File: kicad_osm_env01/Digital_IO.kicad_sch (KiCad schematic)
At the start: 22 parts, among them U18 MIC94073YC6, U20 MIC94073YC6

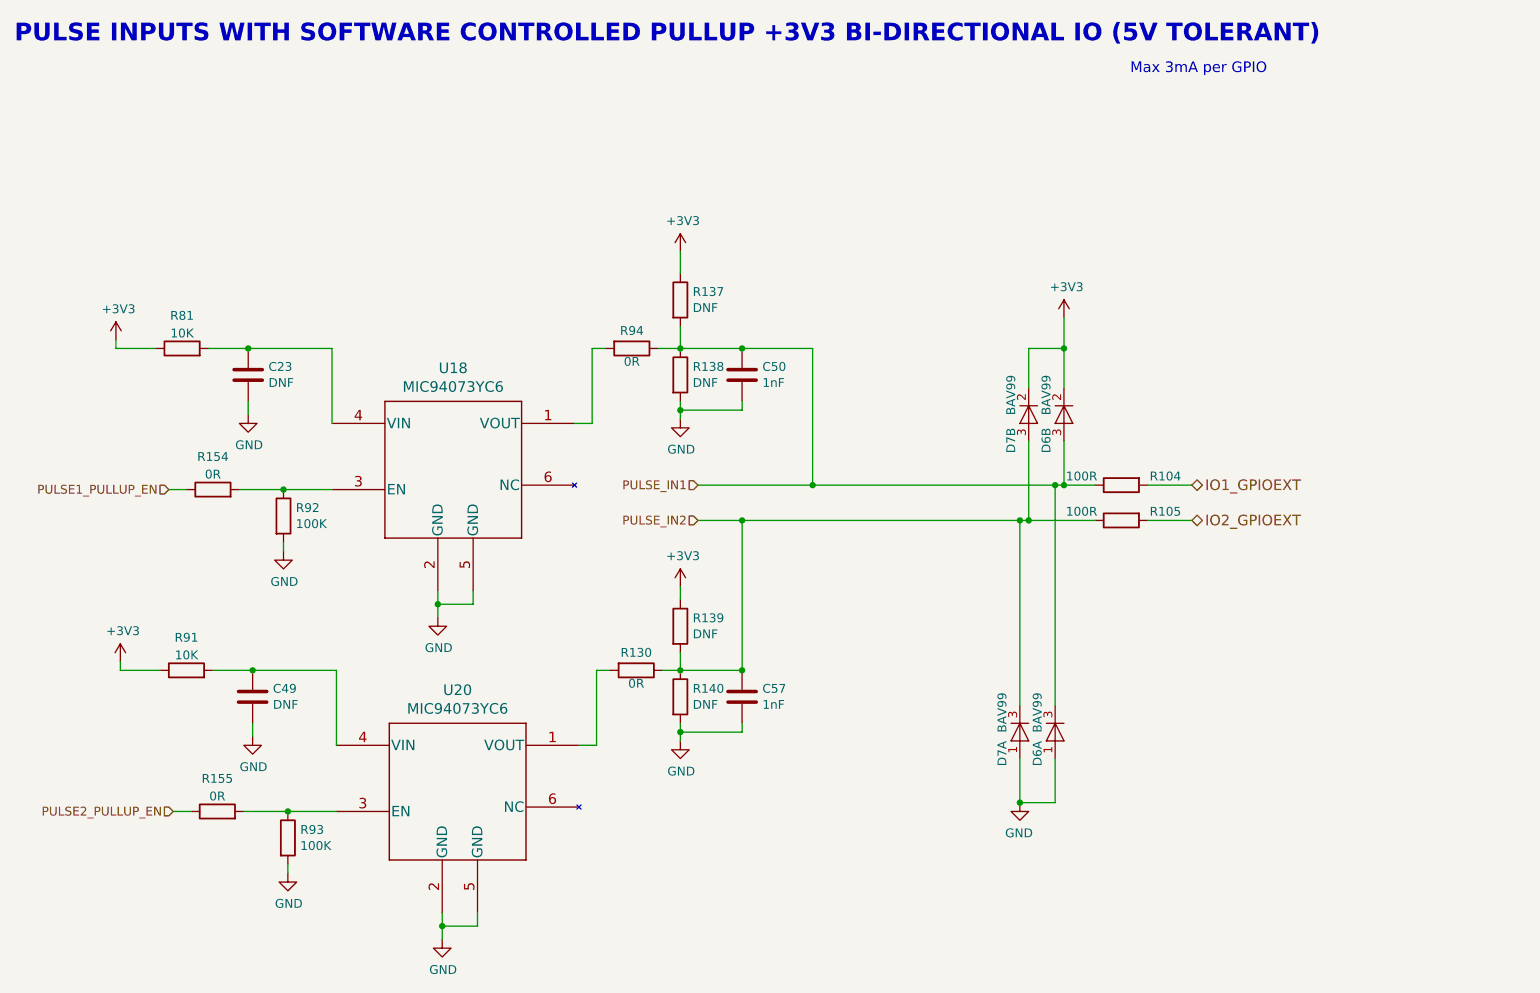
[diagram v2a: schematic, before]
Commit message: updated schematics
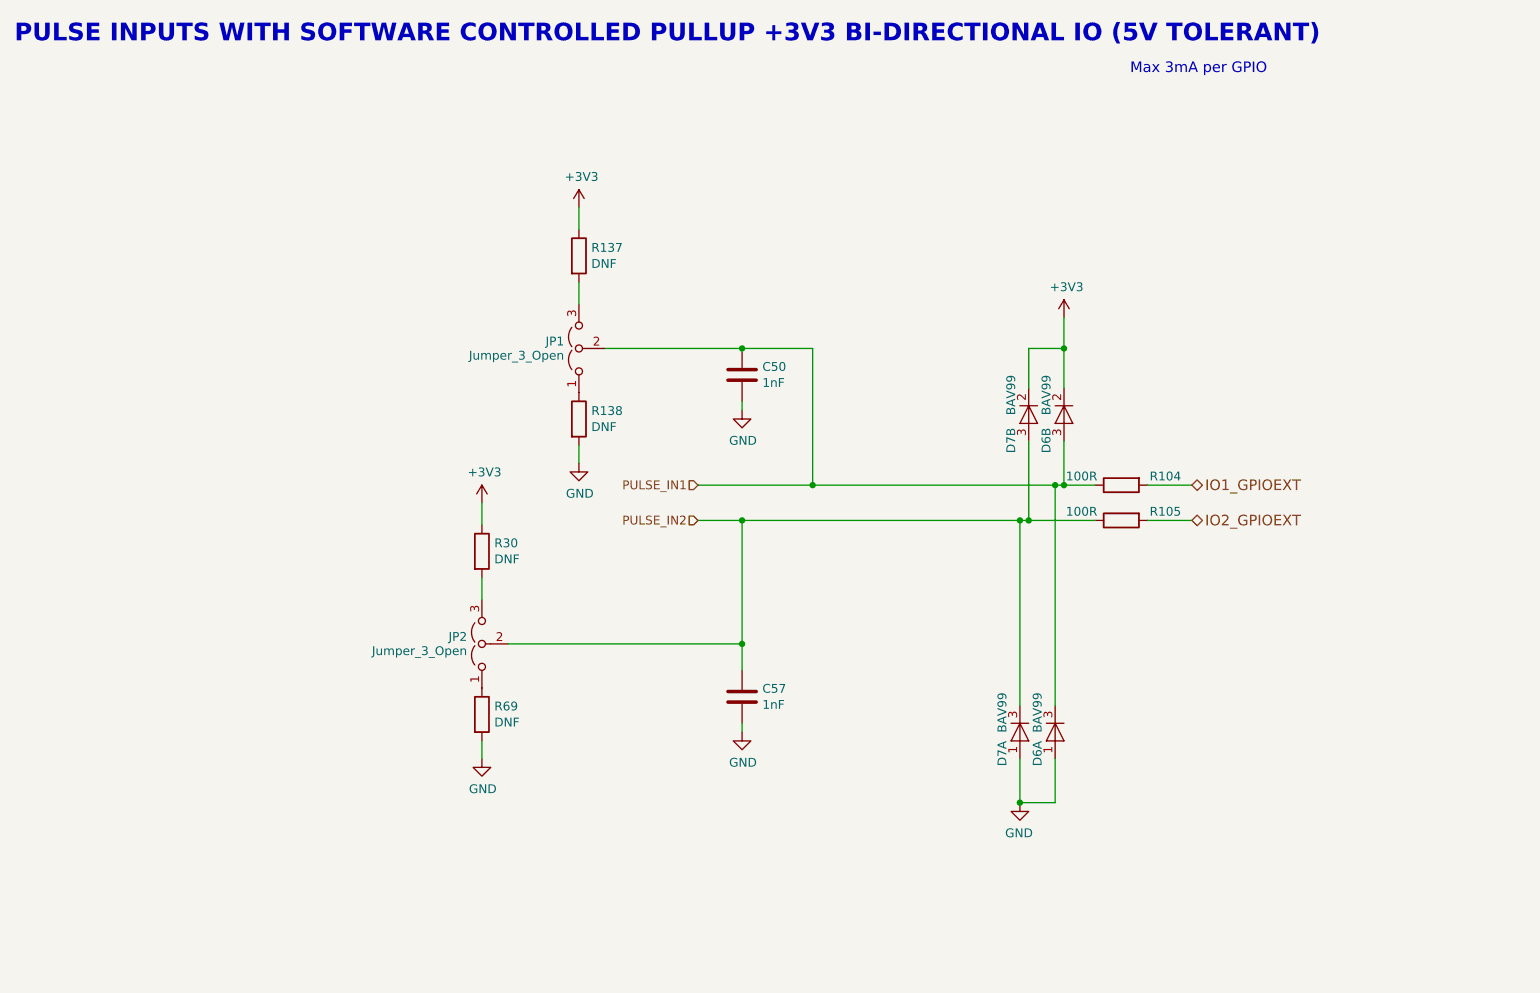
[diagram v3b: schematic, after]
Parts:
- removed C23, C49: DNF, Capacitor_SMD:C_0402_1005Metric, symbol Device:C
- removed R130, R154, R155, R94: 0R, Resistor_SMD:R_0402_1005Metric, symbol Device:R
- removed R139, R140: DNF, Resistor_SMD:R_0402_1005Metric, symbol Device:R
- removed R81, R91: 10K, Resistor_SMD:R_0402_1005Metric, symbol Device:R
- removed R92, R93: 100K, Resistor_SMD:R_0402_1005Metric, symbol Device:R
- removed U18, U20: MIC94073YC6, Package_TO_SOT_SMD:SOT-363_SC-70-6, symbol Devtank:MIC94073YC6
- added JP1, JP2: Jumper_3_Open, symbol Jumper:Jumper_3_Open
- added R30, R69: DNF, Resistor_SMD:R_0402_1005Metric, symbol Device:R
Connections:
- net +3V3: now also R30.1
- net GND: now also R69.2
- net PULSE_IN1: now also JP1.2 (C); no longer R137.2, R138.1
- net PULSE_IN2: now also JP2.2 (C)
- new net: JP2.1 (A), R69.1
- new net: JP2.3 (B), R30.2
- new net: JP1.1 (A), R138.1
- new net: JP1.3 (B), R137.2
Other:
- moved on the sheet: R137, R138

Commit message: added tracking to layout
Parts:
- removed JP1, JP2: Jumper_3_Open, symbol Jumper:Jumper_3_Open
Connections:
- net PULSE_IN1: now also R137.2, R138.1
- net PULSE_IN2: now also R30.2, R69.1
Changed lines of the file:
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@@
   (junction (at 203.835 130.81) (diameter 0) (color 0 0 0 0)
   )
+  (junction (at 140.335 65.405) (diameter 0) (color 0 0 0 0)
+  )
+  (junction (at 126.365 107.95) (diameter 0) (color 0 0 0 0)
+  )
   (junction (at 210.185 85.09) (diameter 0) (color 0 0 0 0)
   )
@@
     (stroke (width 0) (type default))
   )
-  (wire (pts (xy 126.365 98.425) (xy 126.365 101.6))
+  (wire (pts (xy 126.365 98.425) (xy 126.365 107.95))
     (stroke (width 0) (type default))
   )
@@
     (stroke (width 0) (type default))
   )
+  (wire (pts (xy 126.365 107.95) (xy 163.83 107.95))
+    (stroke (width 0) (type default))
+  )
   (wire (pts (xy 163.83 65.405) (xy 173.99 65.405))
     (stroke (width 0) (type default))
@@
     (stroke (width 0) (type default))
   )
-  (wire (pts (xy 144.145 65.405) (xy 163.83 65.405))
+  (wire (pts (xy 140.335 65.405) (xy 163.83 65.405))
     (stroke (width 0) (type default))
   )
@@
     (stroke (width 0) (type default))
   )
+  (wire (pts (xy 140.335 65.405) (xy 140.335 71.755))
+    (stroke (width 0) (type default))
+  )
+  (wire (pts (xy 126.365 107.95) (xy 126.365 114.3))
+    (stroke (width 0) (type default))
+  )
   (wire (pts (xy 210.185 71.12) (xy 210.185 65.405))
     (stroke (width 0) (type default))
@@
     (stroke (width 0) (type default))
   )
-  (wire (pts (xy 140.335 55.88) (xy 140.335 59.055))
+  (wire (pts (xy 140.335 55.88) (xy 140.335 65.405))
     (stroke (width 0) (type default))
   )
@@
   )
   (wire (pts (xy 210.185 65.405) (xy 205.105 65.405))
-    (stroke (width 0) (type default))
-  )
-  (wire (pts (xy 130.175 107.95) (xy 163.83 107.95))
     (stroke (width 0) (type default))
   )
@@
     )
   )
-  (symbol (lib_id "Jumper:Jumper_3_Open") (at 140.335 65.405 90) (unit 1)
-    (in_bom yes) (on_board yes) (dnp no) (fields_autoplaced)
-    (property "Reference" "JP1" (at 138.2009 64.381 90)
-      (effects (font (size 1.27 1.27)) (justify left))
-    )
-    (property "Value" "Jumper_3_Open" (at 138.2009 66.429 90)
-      (effects (font (size 1.27 1.27)) (justify left))
-    )
-    (property "Footprint" "" (at 140.335 65.405 0)
-      (effects (font (size 1.27 1.27)) hide)
-    )
-    (property "Datasheet" "~" (at 140.335 65.405 0)
-      (effects (font (size 1.27 1.27)) hide)
-    )
-    (pin "1")
-    (pin "2")
-    (pin "3")
-    (instances
-      (project "OSM_env01"
-        (path "/ab8b0540-9c9f-4195-88f5-7bed0b0a8ed6/00000000-0000-0000-0000-0000608f4675/00000000-0000-0000-0000-000060920857"
-          (reference "JP1") (unit 1)
-        )
-      )
-    )
-  )
   (symbol (lib_id "power:GND") (at 163.83 74.295 0) (unit 1)
     (in_bom yes) (on_board yes) (dnp no)
@@
         )
       )
-    )
-  )
-  (symbol (lib_id "Jumper:Jumper_3_Open") (at 126.365 107.95 90) (unit 1)
-    (in_bom yes) (on_board yes) (dnp no) (fields_autoplaced)
-    (property "Reference" "JP2" (at 124.2309 106.926 90)
-      (effects (font (size 1.27 1.27)) (justify left))
-    )
-    (property "Value" "Jumper_3_Open" (at 124.2309 108.974 90)
-      (effects (font (size 1.27 1.27)) (justify left))
-    )
-    (property "Footprint" "" (at 126.365 107.95 0)
-      (effects (font (size 1.27 1.27)) hide)
-    )
-    (property "Datasheet" "~" (at 126.365 107.95 0)
-      (effects (font (size 1.27 1.27)) hide)
-    )
-    (pin "1")
-    (pin "2")
-    (pin "3")
-    (instances
-      (project "OSM_env01"
-        (path "/ab8b0540-9c9f-4195-88f5-7bed0b0a8ed6/00000000-0000-0000-0000-0000608f4675/00000000-0000-0000-0000-000060920857"
-          (reference "JP2") (unit 1)
-        )
-      )
